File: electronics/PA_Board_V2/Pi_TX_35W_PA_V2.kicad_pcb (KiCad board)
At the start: 4 copper layers, 100 x 100 mm, 166 parts, among them J1 USB_B_Micro, J10 Conn_01x04, J2 Conn_01x05, J3 Conn_01x05, J4 Conn_01x04, J5 Conn_01x02, J6 Conn_Coaxial, J7 Conn_Coaxial, J8 Conn_Coaxial, J9 Conn_Coaxial, K1 G6E, Q1 AOD4185, Q2 BC848W, Q3 2N7002, SW1 SW_Push, U1 ATSAMD21E18A-A, U10 RA35H1516M, U11 Directional_Coupler, U12 74LV1T34, U2 LM75B, U3 LM2904, U4 LMR51420, U5 MCP4725, U6 AP2204K-ADJ, U7 TLV70233, U8 INA219AxD, U9 ADL5611

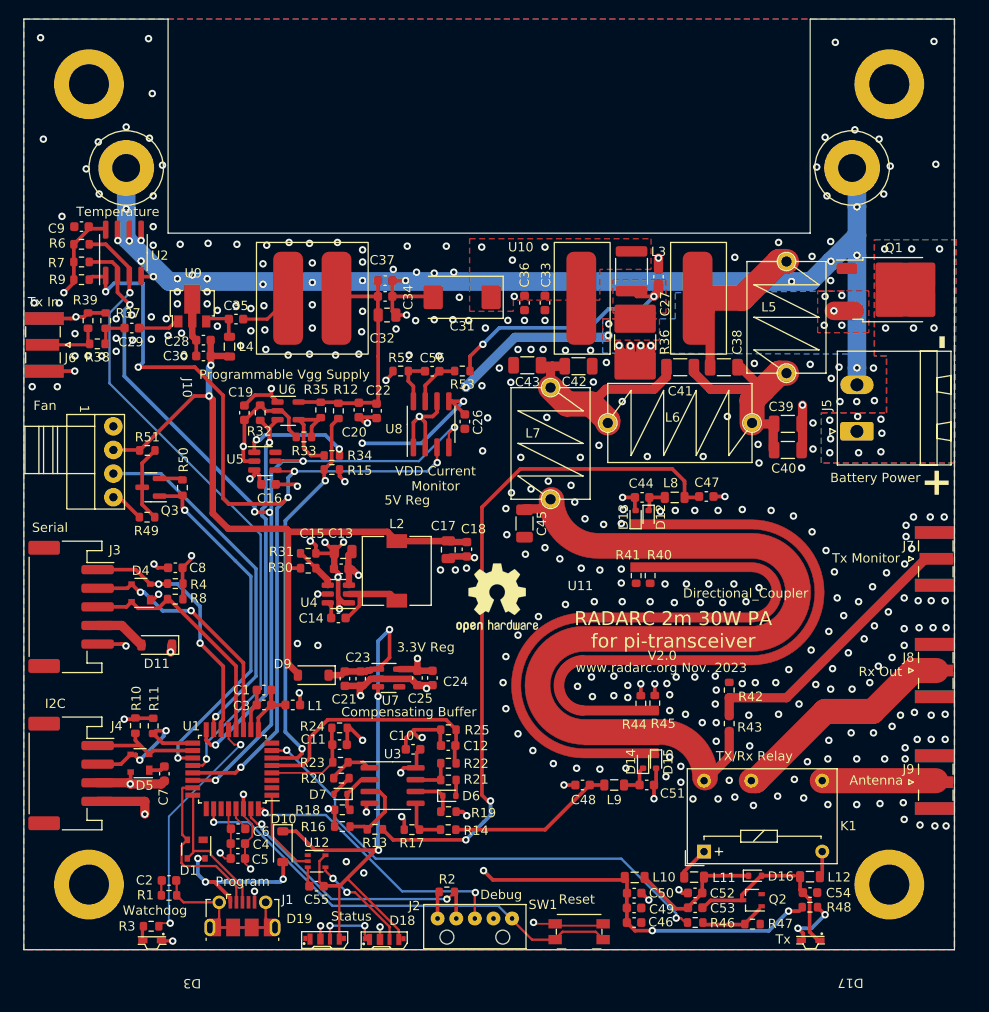
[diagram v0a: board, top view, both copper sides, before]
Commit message: Update PA board V2 Kicad files
New schematic, PCB, and footprints
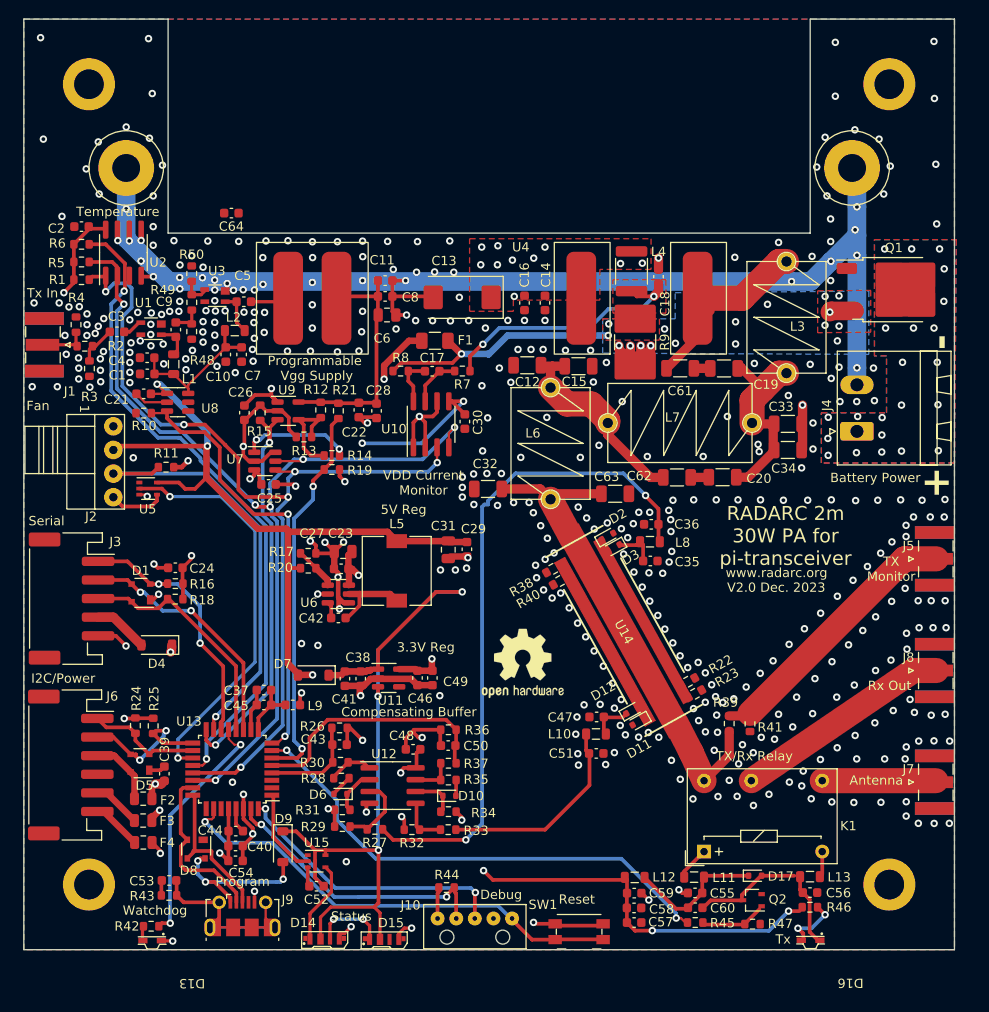
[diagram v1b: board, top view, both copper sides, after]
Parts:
- removed Q3: 2N7002, Package_TO_SOT_SMD:SOT-23
- added C1: 100p, Capacitor_SMD:C_0603_1608Metric, F.Cu at (113.3, 88.1)
- added C21: 1u, Capacitor_SMD:C_0603_1608Metric, F.Cu at (112.9, 90.3)
- added C4: 100n, Capacitor_SMD:C_0603_1608Metric, F.Cu at (113.2, 86.4)
- added C61: 9p1, Capacitor_SMD:C_1206_3216Metric, F.Cu at (170.5, 87.5)
- added C62: 3p, Capacitor_SMD:C_1206_3216Metric, F.Cu at (170.2, 99.2)
- added C63: 6p8, Capacitor_SMD:C_1206_3216Metric, F.Cu at (163.5, 101.0)
- added C64: 330p, Capacitor_SMD:C_0603_1608Metric, F.Cu at (122.3, 70.8)
- added C9: 330p, Capacitor_SMD:C_0603_1608Metric, F.Cu at (116.3, 83.4)
- added F1: 1A, Fuse:Fuse_1206_3216Metric, F.Cu at (144.2, 84.6)
- added F2: 150mA, Fuse:Fuse_0805_2012Metric, F.Cu at (112.8, 133.8)
- added F3: 150mA, Fuse:Fuse_0805_2012Metric, F.Cu at (112.8, 136.1)
- added F4: 150mA, Fuse:Fuse_0805_2012Metric, F.Cu at (112.8, 138.5)
- added L1: 1u, Inductor_SMD:L_0805_2012Metric, F.Cu at (116.1, 87.1)
- added R10: 10k, Resistor_SMD:R_0603_1608Metric, F.Cu at (112.9, 92.3)
- added R48: 300R, Resistor_SMD:R_0603_1608Metric, F.Cu at (118.0, 83.6)
- added U1: PSA4-5043+, Pi_Tx_V2:MM1362 PSA4-5043+, F.Cu at (113.7, 83.3)
- added U5: 74LV1T34, Package_TO_SOT_SMD:SOT-353_SC-70-5, F.Cu at (113.4, 100.5)
- added U8: TPS22810DBV, Package_TO_SOT_SMD:SOT-23-6, F.Cu at (116.5, 91.2)
- C3: renamed from C29; value 10n -> 330p
- H1: renamed from H3; footprint MountingHole:MountingHole_4.3mm_M4_DIN965_Pad -> MountingHole:MountingHole_3.2mm_M3_DIN965_Pad
- H2, H4: footprint MountingHole:MountingHole_4.3mm_M4_DIN965_Pad -> MountingHole:MountingHole_3.2mm_M3_DIN965_Pad
- H3: renamed from H1; footprint MountingHole:MountingHole_4.3mm_M4_DIN965_Pad -> MountingHole:MountingHole_3.2mm_M3_DIN965_Pad
- J6: renamed from J4; value Conn_01x04 -> Conn_01x06; footprint Pi_Tx_V2:JST_PH_S4B-PH-SM4-TB_1x04-1MP_P2.00mm_Horizontal -> Pi_Tx_V2:JST_PH_S6B-PH-SM4-TB_1x06-1MP_P2.00mm_Horizontal
- R2: renamed from R38; value 37.4R -> 18R
- R3: renamed from R39; value 150R -> 300R
- R4: renamed from R37; value 150R -> 300R
- R49: value 2k -> 18R
- R50: value 10k -> 300R
- R7: renamed from R53; value 10k -> 10R
- R8: renamed from R52; value 10k -> 10R
- U14: renamed from U11; footprint Pi_Tx_V2:Wiggly Coupler -> Pi_Tx_V2:Linear_Coupler
- U3: renamed from U9; value ADL5611 -> PSA4-5043+; footprint Package_TO_SOT_SMD:SOT-89-3 -> Pi_Tx_V2:MM1362 PSA4-5043+
- moved R49 23.6 mm to (118.0, 80.4), turned to -90 degrees
- moved R50 23.0 mm to (118.0, 77.3)
- moved C20 12.7 mm to (175.1, 99.2)
- moved R40 9.70 mm to (157.6, 110.4), turned to -151 degrees
- moved C47 9.08 mm to (161.6, 125.0), turned to 180 degrees
- moved R38 8.94 mm to (156.9, 109.1), turned to -151 degrees
- moved LOGO1 7.55 mm to (153.6, 119.2)
- moved C35 6.89 mm to (167.3, 108.2), turned to 0 degrees
- moved C36 6.63 mm to (167.4, 104.3), turned to 180 degrees
- moved L10 5.82 mm to (161.5, 126.8)
- moved D12 5.64 mm to (165.3, 124.3), turned to 29 degrees
- moved R22 5.58 mm to (171.4, 121.2), turned to -151 degrees
- moved L8 5.45 mm to (167.3, 106.2)
- moved R3 5.45 mm to (107.0, 87.6), turned to -90 degrees
- moved C32 5.40 mm to (149.9, 100.5), turned to 180 degrees
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- renumbered C28 to C10, C37 to C11, C43 to C12, C31 to C13, C33 to C14, C42 to C15, C36 to C16, C56 to C17, C27 to C18, C38 to C19, C9 to C2, C41 to C20, C20 to C22, C13 to C23, C8 to C24, C16 to C25, C19 to C26, C15 to C27, C22 to C28, C18 to C29, C26 to C30, C17 to C31, C45 to C32, C39 to C33, C40 to C34, C44 to C35, C47 to C36, C1 to C37, C23 to C38, C7 to C39, C4 to C40, C21 to C41, C14 to C42, C11 to C43, C6 to C44, C3 to C45, C25 to C46, C51 to C47, C10 to C48, C24 to C49, C35 to C5, C12 to C50, C48 to C51, C55 to C52, C2 to C53, C5 to C54, C52 to C55, C54 to C56, C46 to C57, C49 to C58, C50 to C59, C32 to C6, C53 to C60, C30 to C7, C34 to C8, D4 to D1, D6 to D10, D15 to D11, D14 to D12, D3 to D13, D19 to D14, D18 to D15, D17 to D16, D16 to D17, D13 to D2, D12 to D3, D11 to D4, D7 to D6, D9 to D7, D1 to D8, D10 to D9, J6 to J1, J2 to J10, J10 to J2, J5 to J4, J7 to J5, J9 to J7, J1 to J9, L9 to L10, L10 to L12, L12 to L13, L4 to L2, L5 to L3, L3 to L4, L2 to L5, L7 to L6, L6 to L7, L1 to L9, R9 to R1, R51 to R11, R35 to R12, R33 to R13, R34 to R14, R32 to R15, R4 to R16, R31 to R17, R8 to R18, R15 to R19, R30 to R20, R12 to R21, R44 to R22, R45 to R23, R10 to R24, R11 to R25, R24 to R26, R13 to R27, R20 to R28, R16 to R29, R23 to R30, R18 to R31, R17 to R32, R14 to R33, R19 to R34, R21 to R35, R25 to R36, R22 to R37, R41 to R38, R42 to R39, R43 to R41, R3 to R42, R1 to R43, R2 to R44, R46 to R45, R48 to R46, R7 to R5, R36 to R9, U8 to U10, U7 to U11, U3 to U12, U1 to U13, U12 to U15, U10 to U4, U4 to U6, U5 to U7, U6 to U9
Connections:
- C10 pad 2: +5V -> Net-(U8-VOUT)
- C12 pad 1: Net-(C41-Pad2) -> Net-(C12-Pad1)
- C15 pad 1: Net-(C41-Pad2) -> Net-(C12-Pad1)
- C19 pad 1: Net-(U10-RF_Out) -> Net-(C19-Pad1)
- C20 pad 2: Net-(C41-Pad2) -> Net-(C20-Pad2)
- C3 pad 1: Net-(C29-Pad1) -> Net-(C3-Pad1)
- C5 pad 2: Net-(C35-Pad2) -> Net-(C5-Pad2)
- C7 pad 2: +5V -> Net-(U8-VOUT)
- D14 pad 1: unconnected-(D19-DOUT-Pad1) -> Net-(D14-DIN)
- D14 pad 2: GND -> VDC
- D14 pad 4: VDC -> GND
- D15 pad 2: GND -> VDC
- D15 pad 3: Net-(D18-DIN) -> unconnected-(D15-DOUT-Pad3)
- D15 pad 4: VDC -> GND
- D2 pad 1: Net-(D12-A) -> Net-(D2-K)
- D3 pad 2: Net-(D12-A) -> Net-(D2-K)
- D5 pad 4: +3.3V -> Net-(J6-Pin_3)
- J2 pad 4: Net-(J10-Pin_4) -> Net-(J2-Pin_4)
- J6 pad 3: +3.3V -> Net-(J6-Pin_3)
- L2 pad 1: +5V -> Net-(U8-VOUT)
- L2 pad 2: Net-(C35-Pad2) -> Net-(C5-Pad2)
- L3 pad 1: Net-(U10-RF_Out) -> Net-(U4-RF_Out)
- L6 pad 1: Net-(C41-Pad2) -> Net-(C12-Pad1)
- L7 pad 2: Net-(C41-Pad2) -> Net-(C12-Pad1)
- Q1 pad 3: +12V -> /PA_Power/VBAT
- R11 pad 1: +5V -> +3.3V
- R11 pad 2: Net-(Q3-D) -> /PA_Protection/Fan_RPM
- R22 pad 2: Net-(D12-A) -> Net-(U14-Fterm)
- R23 pad 2: Net-(D12-A) -> Net-(U14-Fterm)
- R49 pad 1: Net-(J10-Pin_4) -> Net-(C64-Pad2)
- R49 pad 2: Net-(Q3-D) -> Net-(C9-Pad1)
- R50 pad 1: /PA_Protection/Fan PWM -> Net-(C64-Pad2)
- R8 pad 1: +12V -> /PA_Power/VBAT
- R9 pad 2: +12V -> /PA_Power/VBAT
- U13 pad 8: unconnected-(U1-PA07-Pad8) -> /PA_Protection/DRIVER_EN
- U14 pad 2: Net-(D12-A) -> Net-(D2-K)
- U15 pad 4: Net-(D18-DIN) -> Net-(D14-DIN)
- U3 pad 1: Net-(C29-Pad1) -> Net-(C5-Pad2)
- U3 pad 3: Net-(C35-Pad2) -> Net-(C64-Pad1)
- U4 pad 4: Net-(U10-RF_Out) -> Net-(U4-RF_Out)
- U7 pad 6: unconnected-(U5-A0-Pad6) -> GND
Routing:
- net /PA_Protection/DRIVER_EN: track 0.00 -> 47.6 mm, vias 0 -> 2
- net /PA_Power/VBAT: track 0.00 -> 40.1 mm, vias 0 -> 15
- net +5V: track 79.7 -> 109.6 mm, vias 2 -> 4
- net GND: track 283.5 -> 256.4 mm, vias 351 -> 415
- net Net-(C41-Pad2): track 23.0 -> 0.00 mm
- net Net-(U4-RF_Out): track 0.00 -> 22.0 mm
- net Net-(C12-Pad1): track 0.00 -> 21.8 mm
- net Net-(U14-RF): track 9.73 -> 29.8 mm
- net Net-(U10-RF_Out): track 19.2 -> 0.00 mm
- net Net-(U8-VOUT): track 0.00 -> 17.0 mm
- net VDC: track 96.9 -> 112.3 mm
- net Net-(D18-DIN): track 11.1 -> 0.00 mm, vias 2 -> 0
- net Net-(D14-DIN): track 0.00 -> 8.94 mm
- net /PA_Protection/Fan_RPM: track 38.7 -> 47.1 mm
- net Net-(Q3-D): track 8.30 -> 0.00 mm
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- added copper zone on B.Cu, net /PA_Power/VBAT
- added copper zone on F.Cu, net /PA_Power/VBAT
- added copper zone on In1.Cu, net /PA_Power/VBAT
- added copper zone on In2.Cu, net /PA_Power/VBAT
- removed copper zone on B.Cu, net +12V
- removed copper zone on F.Cu, net +12V
- removed copper zone on In1.Cu, net +12V
- removed copper zone on In2.Cu, net +12V
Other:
- board text added: "I2C/Power"
- board text added: "TX Monitor"
- board text added: "V2.0 Dec. 2023"
- board text added: "www.radarc.org"
- board text removed: "I2C"
- board text removed: "Tx Monitor"
- board text removed: "V2.0"
- board text removed: "www.radarc.org Nov. 2023"

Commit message: Save unlocked Kicad files for PA Board V2
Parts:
- moved C64 7.49 mm to (118.8, 77.5)
- moved R50 1.90 mm to (116.4, 78.3), turned to -90 degrees
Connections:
- R22 pad 2: Net-(U14-Fterm) -> Net-(D2-K)
- R23 pad 2: Net-(U14-Fterm) -> Net-(D2-K)
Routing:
- net GND: track 256.4 -> 275.1 mm, vias 415 -> 419
- net Net-(C64-Pad2): track 0.00 -> 3.81 mm
- net (no net): track 3.21 -> 0.00 mm
- net Net-(C64-Pad1): track 0.00 -> 1.66 mm

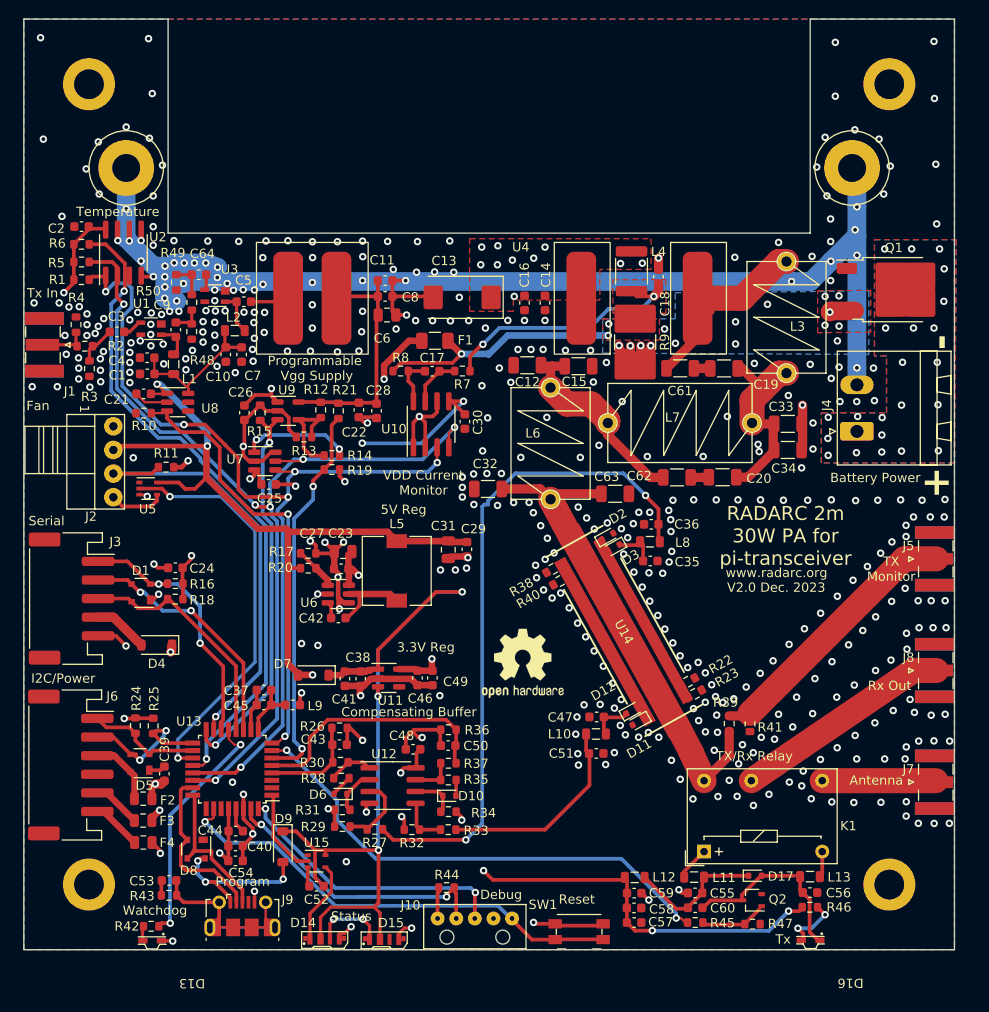
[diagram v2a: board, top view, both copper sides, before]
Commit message: Update Arduino documentation and change to Kicad V8
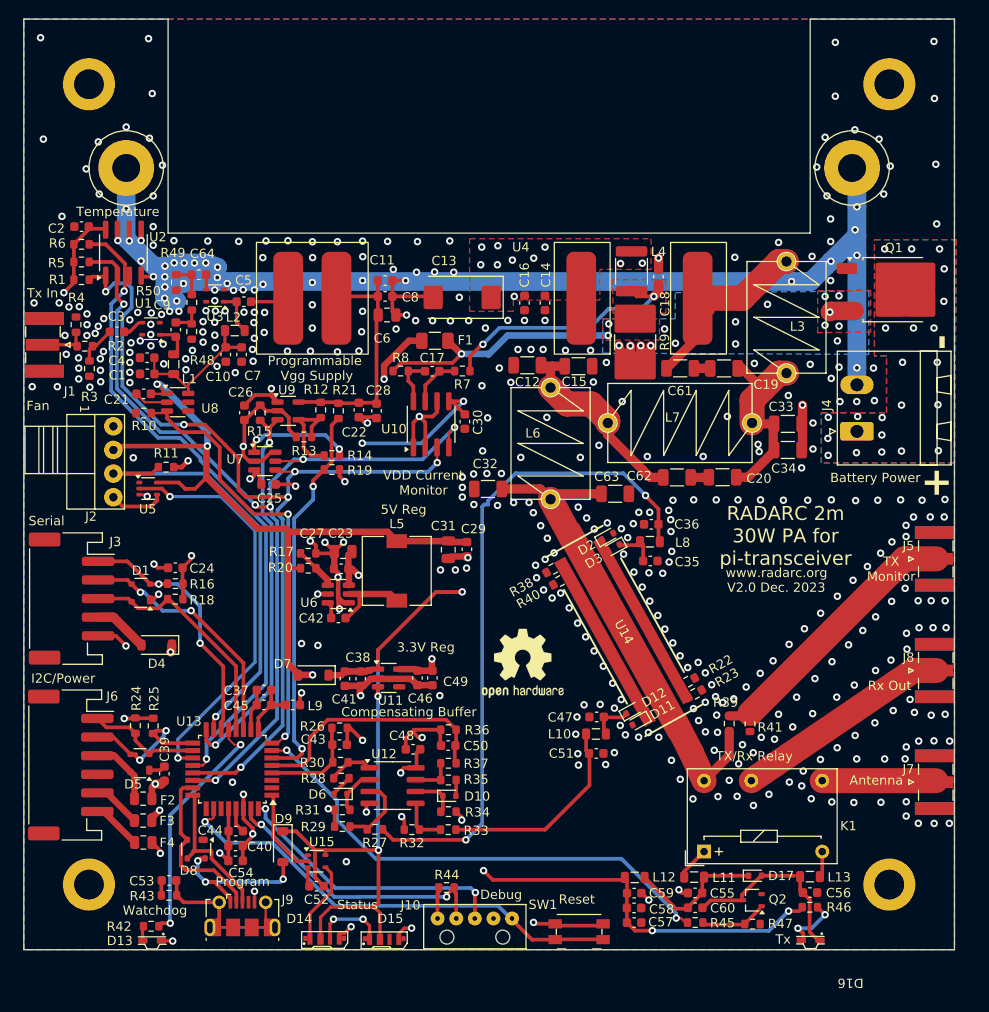
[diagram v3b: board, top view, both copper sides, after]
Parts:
- U1, U3: footprint Pi_Tx_V2:MM1362 PSA4-5043+ -> Package_TO_SOT_SMD:SOT-343_SC-70-4
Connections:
- C32 pad 1: Net-(U14-RF) -> Net-(U14-RF)_1
- C63 pad 1: Net-(U14-RF) -> Net-(U14-RF)_1
- L6 pad 2: Net-(U14-RF) -> Net-(U14-RF)_1
- R22 pad 2: Net-(D2-K) -> Net-(U14-Fterm)
- R23 pad 2: Net-(D2-K) -> Net-(U14-Fterm)
- R38 pad 1: Net-(D11-K) -> Net-(U14-Rterm)
- R40 pad 1: Net-(D11-K) -> Net-(U14-Rterm)
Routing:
- net Net-(U14-RF)_1: track 0.00 -> 16.3 mm
- net Net-(U14-RF): track 29.8 -> 13.5 mm

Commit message: Updates in electronics bits and bobs
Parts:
- added F5: 150mA, Fuse:Fuse_0805_2012Metric, F.Cu at (119.2, 104.6)
- added F6: 150mA, Fuse:Fuse_0805_2012Metric, F.Cu at (119.2, 102.4)
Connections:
- C32 pad 1: Net-(U14-RF)_1 -> Net-(U14-RF)
- C63 pad 1: Net-(U14-RF)_1 -> Net-(U14-RF)
- J2 pad 2: +5V -> Net-(J2-Pin_2)
- K1 pad 12: Net-(U14-RF) -> Net-(U14-RF)_1
- L6 pad 2: Net-(U14-RF)_1 -> Net-(U14-RF)
- R41 pad 2: Net-(U14-RF) -> Net-(U14-RF)_1
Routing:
- net Net-(J2-Pin_2): track 0.00 -> 22.7 mm, vias 0 -> 1
- net +12V: track 175.7 -> 192.9 mm, vias 8 -> 9
- net +5V: track 109.6 -> 100.9 mm
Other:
- board text added: "12V"
- board text added: "5V"
